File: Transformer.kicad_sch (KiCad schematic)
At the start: 3 parts

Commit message: added some kind of PCB design, a rough draft
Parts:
- TR1, TR2, TR3: footprint (none) -> Transformer_THT:Transformer_NF_ETAL_1-1_P1200
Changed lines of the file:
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@@
 			)
 		)
-		(property "Footprint" ""
+		(property "Footprint" "Transformer_THT:Transformer_NF_ETAL_1-1_P1200"
 			(at 137.16 116.84 0)
 			(effects
@@
 			)
 		)
-		(property "Footprint" ""
+		(property "Footprint" "Transformer_THT:Transformer_NF_ETAL_1-1_P1200"
 			(at 137.16 76.2 0)
 			(effects
@@
 			)
 		)
-		(property "Footprint" ""
+		(property "Footprint" "Transformer_THT:Transformer_NF_ETAL_1-1_P1200"
 			(at 137.16 96.52 0)
 			(effects

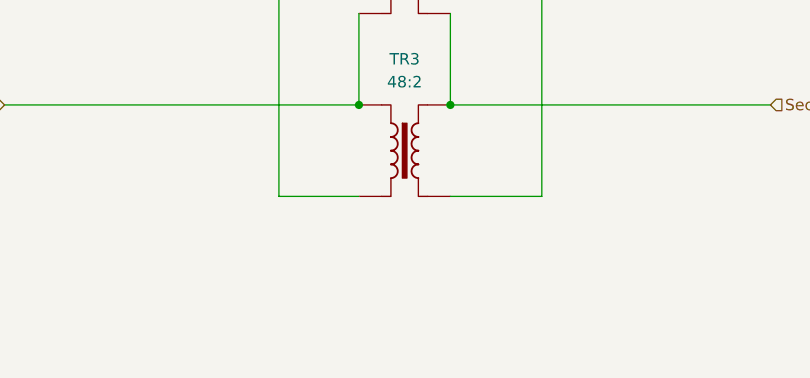
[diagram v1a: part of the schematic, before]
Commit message: Updates to Secondary side for PCB
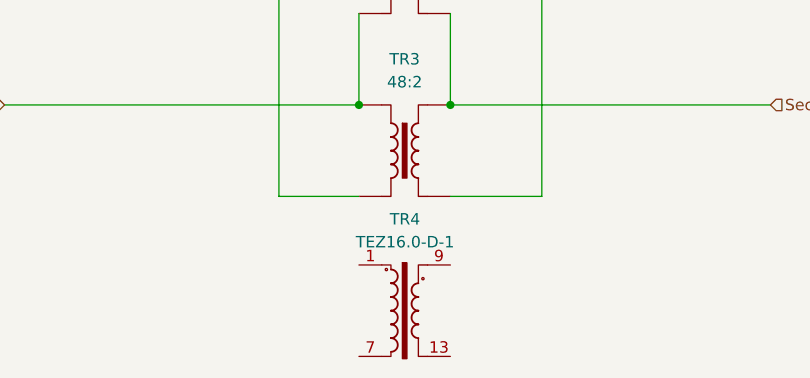
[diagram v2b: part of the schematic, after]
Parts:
- added TR4: TEZ16.0-D-1, Transformer_THT:Transformer_Breve_TEZ-47x57, symbol Transformer:TEZ16.0-D-1
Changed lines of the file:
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@@
+	)
+	(symbol
+		(lib_id "Transformer:TEZ16.0-D-1")
+		(at 137.16 134.62 0)
+		(unit 1)
+		(exclude_from_sim no)
+		(in_bom yes)
+		(on_board yes)
+		(dnp no)
+		(fields_autoplaced yes)
+		(property "Reference" "TR4"
+			(at 137.1981 124.46 0)
+			(effects
+				(font
+					(size 1.27 1.27)
+				)
+			)
+		)
+		(property "Value" "TEZ16.0-D-1"
+			(at 137.1981 127 0)
+			(effects
+				(font
+					(size 1.27 1.27)
+				)
+			)
+		)
+		(property "Footprint" "Transformer_THT:Transformer_Breve_TEZ-47x57"
+			(at 137.16 143.51 0)
+			(effects
+				(font
+					(size 1.27 1.27)
+					(italic yes)
+				)
+				(hide yes)
+			)
+		)
+		(property "Datasheet" "http://www.breve.pl/pdf/ANG/TEZ_ang.pdf"
+			(at 137.16 134.62 0)
+			(effects
+				(font
+					(size 1.27 1.27)
+				)
+				(hide yes)
+			)
+		)
+		(property "Description" "TEZ16.0/D/x, 16VA, Single Secondary, Cast Resin Transformer, PCB"
+			(at 137.16 134.62 0)
+			(effects
+				(font
+					(size 1.27 1.27)
+				)
+				(hide yes)
+			)
+		)
+		(pin "13"
+		)
+		(pin "7"
+		)
+		(pin "9"
+		)
+		(pin "1"
+		)
+		(instances
+			(project ""
+				(path "/eaeaab39-7712-4bb8-8f1a-3ddca096a313/4f1abc31-25e4-43c9-b2d8-a8d91b457a44"
+					(reference "TR4")
+					(unit 1)
+				)
+			)
+		)
 	)
 	(symbol
@@
 		(exclude_from_sim no)
 		(in_bom yes)
-		(on_board yes)
+		(on_board no)
 		(dnp no)
 		(fields_autoplaced yes)
@@
 		(exclude_from_sim no)
 		(in_bom yes)
-		(on_board yes)
+		(on_board no)
 		(dnp no)
 		(fields_autoplaced yes)
@@
 		(exclude_from_sim no)
 		(in_bom yes)
-		(on_board yes)
-		(dnp no)
-		(fields_autoplaced yes)
+		(on_board no)
+		(dnp no)
+		(fields_autoplaced yes)

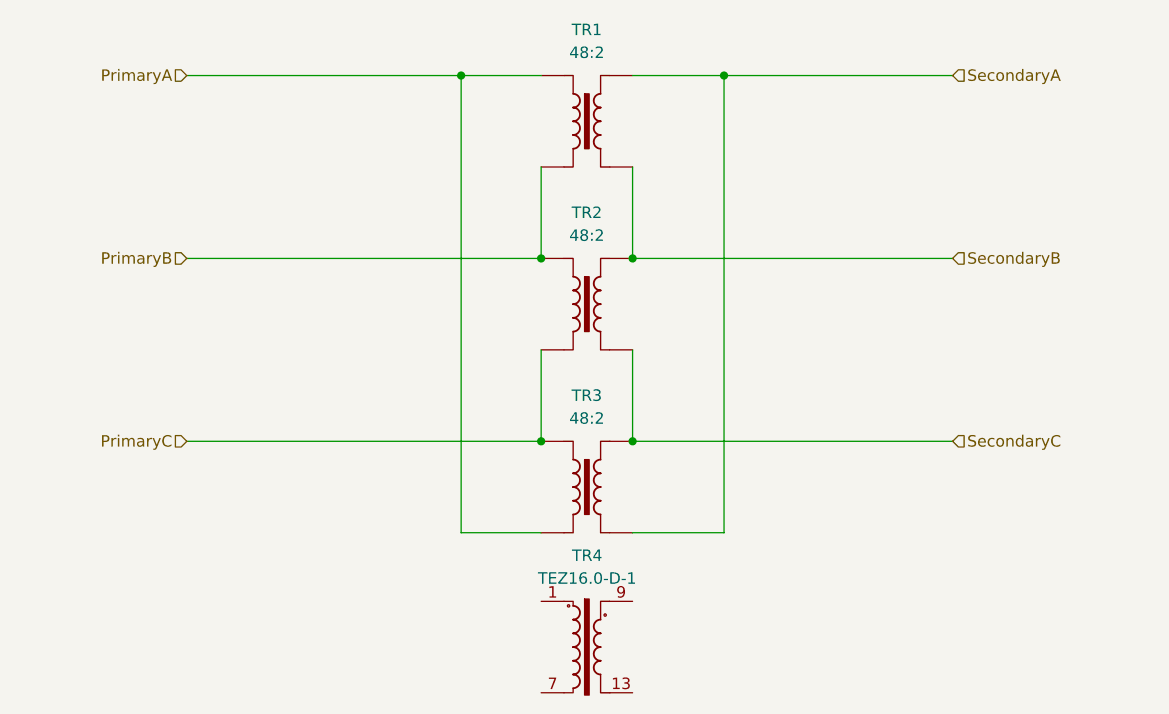
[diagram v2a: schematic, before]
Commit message: nu er vi meget tættere på, den 3 fasede transformer er placeret og interegeret korrekt, sekundær siden er sat, spoler og mosfets, ved ikke om det er det rigtige at gøre men sådan er det jo
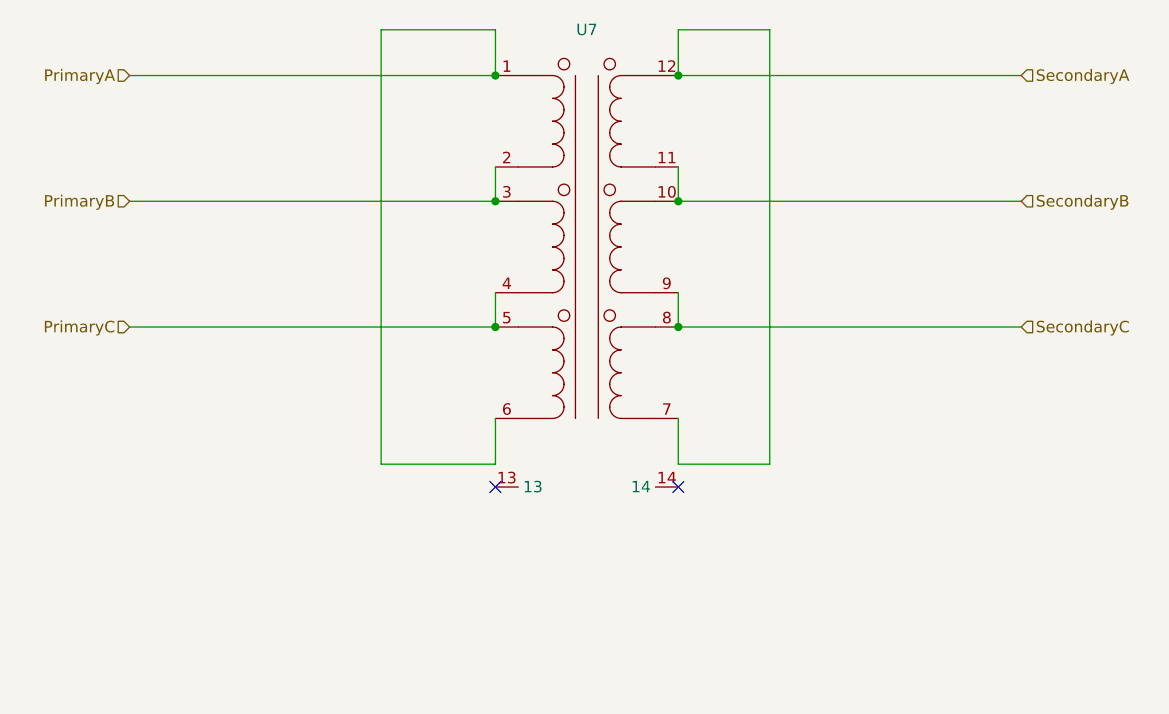
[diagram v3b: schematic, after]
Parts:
- removed TR1, TR2, TR3: 48:2, Transformer_THT:Transformer_NF_ETAL_1-1_P1200, symbol Transformer:TRANSF1
- removed TR4: TEZ16.0-D-1, Transformer_THT:Transformer_Breve_TEZ-47x57, symbol Transformer:TEZ16.0-D-1
- added U7: ~, Transformer_THT:Transformer_Breve_TEZ-47x57, symbol stm:3 Phase transformer
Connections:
- net PrimaryA: now also U7.1, U7.6
- net PrimaryB: now also U7.2, U7.3
- net PrimaryC: now also U7.4, U7.5
- net SecondaryA: now also U7.12, U7.7
- net SecondaryB: now also U7.10, U7.11
- net SecondaryC: now also U7.8, U7.9
- no-connect marks 0 -> 2
